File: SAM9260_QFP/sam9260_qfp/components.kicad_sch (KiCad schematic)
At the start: 64 parts, among them J201 USB_B_Micro, J202 Micro_SD_Card, J203 RJ45, U201 USBLC6-2SC6, U202 LD1117S33TR_SOT223, U203 RTL8211EG-VB-CG, Y201 25Mhz

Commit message: Completed component placing
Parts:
- added C235: 100n, Capacitor_SMD:C_0402_1005Metric, symbol Device:C_Small
- FB201: footprint Inductor_SMD:L_0805_2012Metric -> Inductor_SMD:L_0603_1608Metric
- XMER201: footprint My_First_PCB:H5007NL_PUL -> H5007NL:H5007NL_PUL
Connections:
- net GND is gone; now on net +1V0: C201.2, C202.2, C203.2, C204.2, C205.2, C206.2, C207.2, C208.2, C209.2, C210.2, C211.2, C212.2, C213.2, C214.2, C215.2, C216.2, C217.2, C218.1, C219.2, C220.2, C221.2, C222.2, C223.2, C224.2, C225.1, C226.1, C226.2, C227.2, C228.1, C228.2, C229.2, C230.2, C231.2, C232.2, C233.2, C234.2, J201.5 (GND), J201.6 (Shield), J202.4 (VDD), J202.6 (VSS), L201.2, R203.1, R206.2, R207.2, U201.2 (GND), U202.1 (GND), U203.10 (AVDD33), U203.13 (AVDD10), U203.2 (GND), U203.20 (DVDD33), U203.26 (DVDD33), U203.33 (DVDD10), U203.37 (DVDD33), U203.4 (GND), U203.48 (DVDD10), U203.49 (DVDD33), U203.59 (AVDD10), U203.60 (AVDD33), U203.63 (GND), U203.64 (VDDREG), U203.65 (GND), U203.7 (AVDD10)
- net +1V0: now reaches C220.1, C223.1, C227.1
- net +1V0: now also C229.1, C230.1, C231.1, C235.1, C235.2
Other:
- moved on the sheet: C220, C223, C227

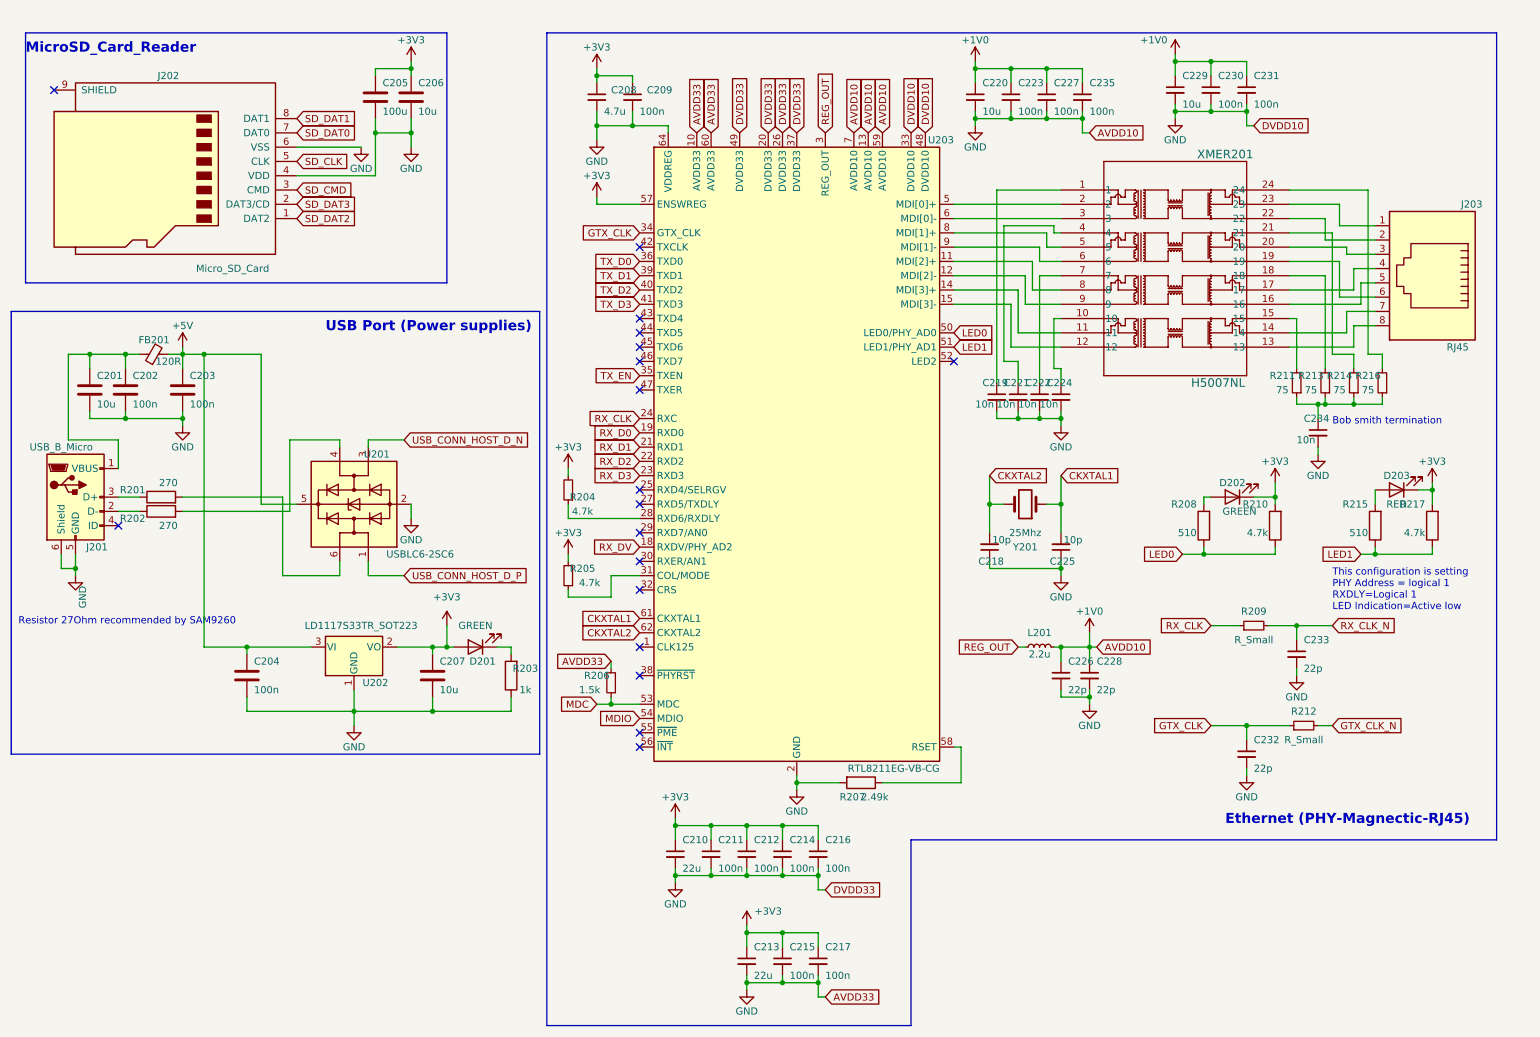
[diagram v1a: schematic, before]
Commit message: updated layout
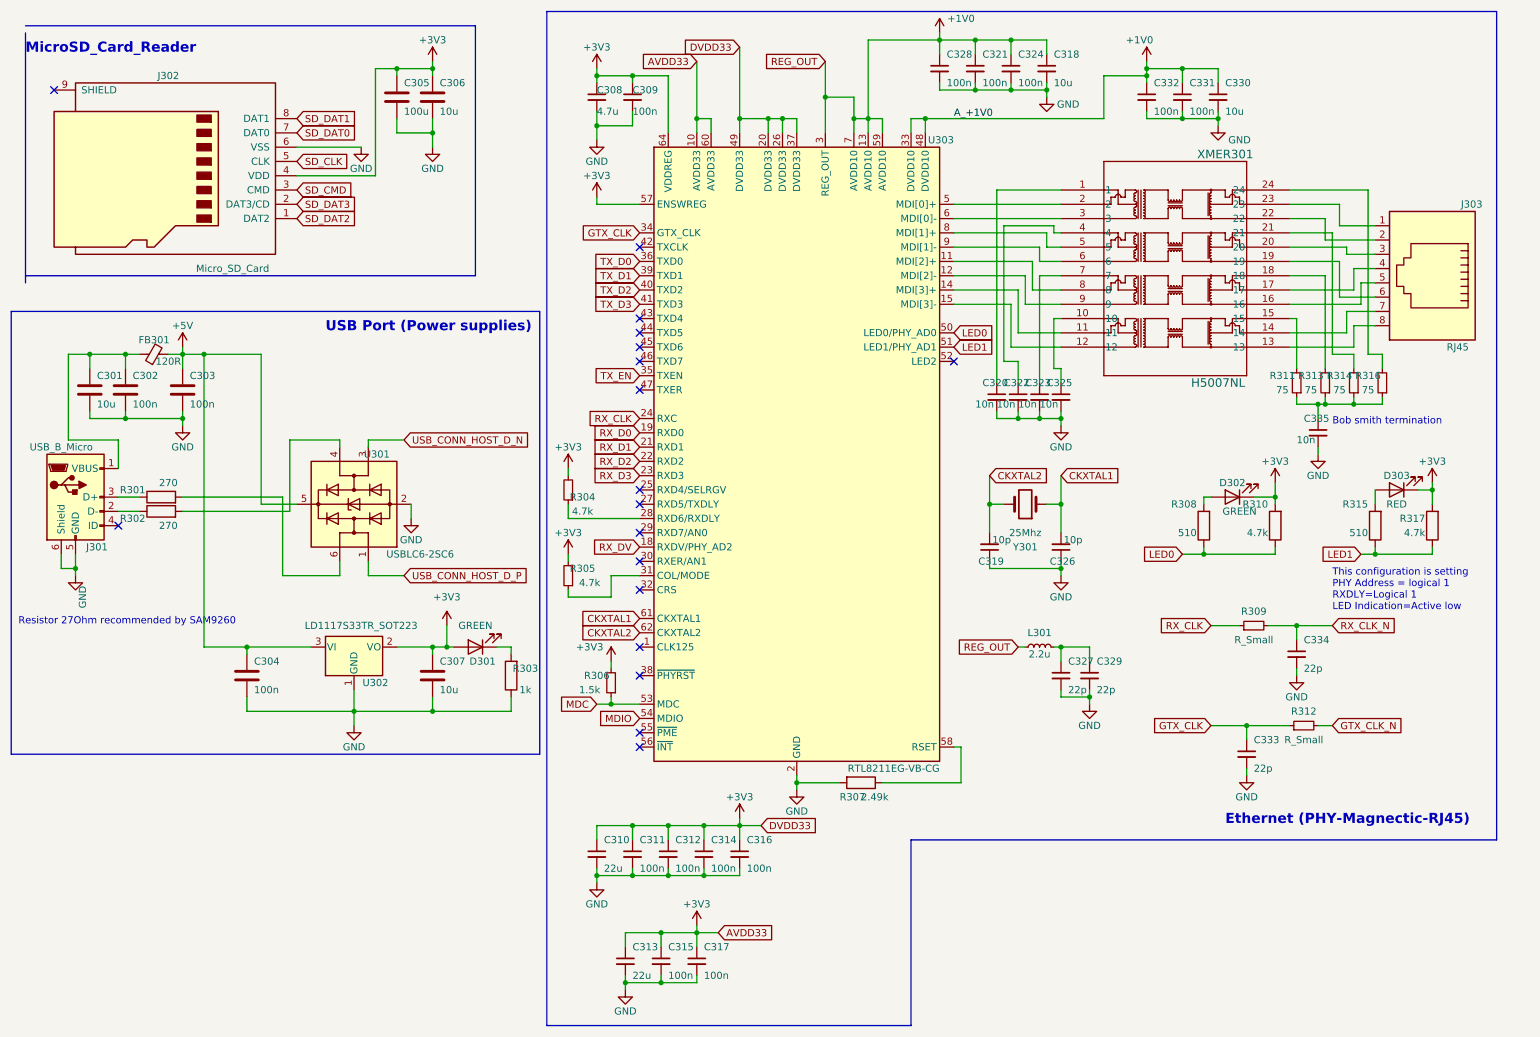
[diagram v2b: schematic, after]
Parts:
- XMER301: renamed from XMER201; footprint H5007NL:H5007NL_PUL -> HL5007:H5007NL_PUL
- renumbered C201 to C301, C202 to C302, C203 to C303, C204 to C304, C205 to C305, C206 to C306, C207 to C307, C208 to C308, C209 to C309, C210 to C310, C211 to C311, C212 to C312, C213 to C313, C214 to C314, C215 to C315, C216 to C316, C217 to C317, C220 to C318, C218 to C319, C219 to C320, C223 to C321, C221 to C322, C222 to C323, C227 to C324, C224 to C325, C225 to C326, C226 to C327, C235 to C328, C228 to C329, C229 to C330, C230 to C331, C231 to C332, C232 to C333, C233 to C334, C234 to C335, D201 to D301, D202 to D302, D203 to D303, FB201 to FB301, J201 to J301, J202 to J302, J203 to J303, L201 to L301, R201 to R301, R202 to R302, R203 to R303, R204 to R304, R205 to R305, R206 to R306, R207 to R307, R208 to R308, R209 to R309, R210 to R310, R211 to R311, R212 to R312, R213 to R313, R214 to R314, R215 to R315, R216 to R316, R217 to R317, U201 to U301, U202 to U302, U203 to U303, Y201 to Y301
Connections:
- net REG_OUT is gone; now on net +1V0: L301.1, U303.3 (REG_OUT)
- net +1V0: no longer C301.2, C302.2, C303.2, C304.2, C305.2, C306.2, C307.2, C308.2, C309.2, C310.2, C311.2, C312.2, C313.2, C314.2, C315.2, C316.2, C317.2, C318.2, C319.1, C320.2, C321.2, C322.2, C323.2, C324.2, C325.2, C326.1, C327.1, C327.2, C328.2, C329.1, C329.2, C330.2, C331.2, C332.2, C333.2, C334.2, C335.2, J301.5 (GND), J301.6 (Shield), J302.4 (VDD), J302.6 (VSS), L301.2, R303.1, R306.2, R307.2, U301.2 (GND), U302.1 (GND), U303.10 (AVDD33), U303.2 (GND), U303.20 (DVDD33), U303.26 (DVDD33), U303.37 (DVDD33), U303.4 (GND), U303.49 (DVDD33), U303.60 (AVDD33), U303.63 (GND), U303.64 (VDDREG), U303.65 (GND)
- net +3V3: now also J302.4 (VDD), R306.2, U303.10 (AVDD33), U303.20 (DVDD33), U303.26 (DVDD33), U303.37 (DVDD33), U303.49 (DVDD33), U303.60 (AVDD33), U303.64 (VDDREG)
- new net: C327.1, C329.1, L301.2
- new net GND: C301.2, C302.2, C303.2, C304.2, C305.2, C306.2, C307.2, C308.2, C309.2, C310.2, C311.2, C312.2, C313.2, C314.2, C315.2, C316.2, C317.2, C318.2, C319.1, C320.2, C321.2, C322.2, C323.2, C324.2, C325.2, C326.1, C327.2, C328.2, C329.2, C330.2, C331.2, C332.2, C333.2, C334.2, C335.2, J301.5 (GND), J301.6 (Shield), J302.6 (VSS), R303.1, R307.2, U301.2 (GND), U302.1 (GND), U303.2 (GND), U303.4 (GND), U303.63 (GND), U303.65 (GND)
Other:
- moved on the sheet: C305, C306, C310, C311, C312, C313, C314, C315, C316, C317, C318, C321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

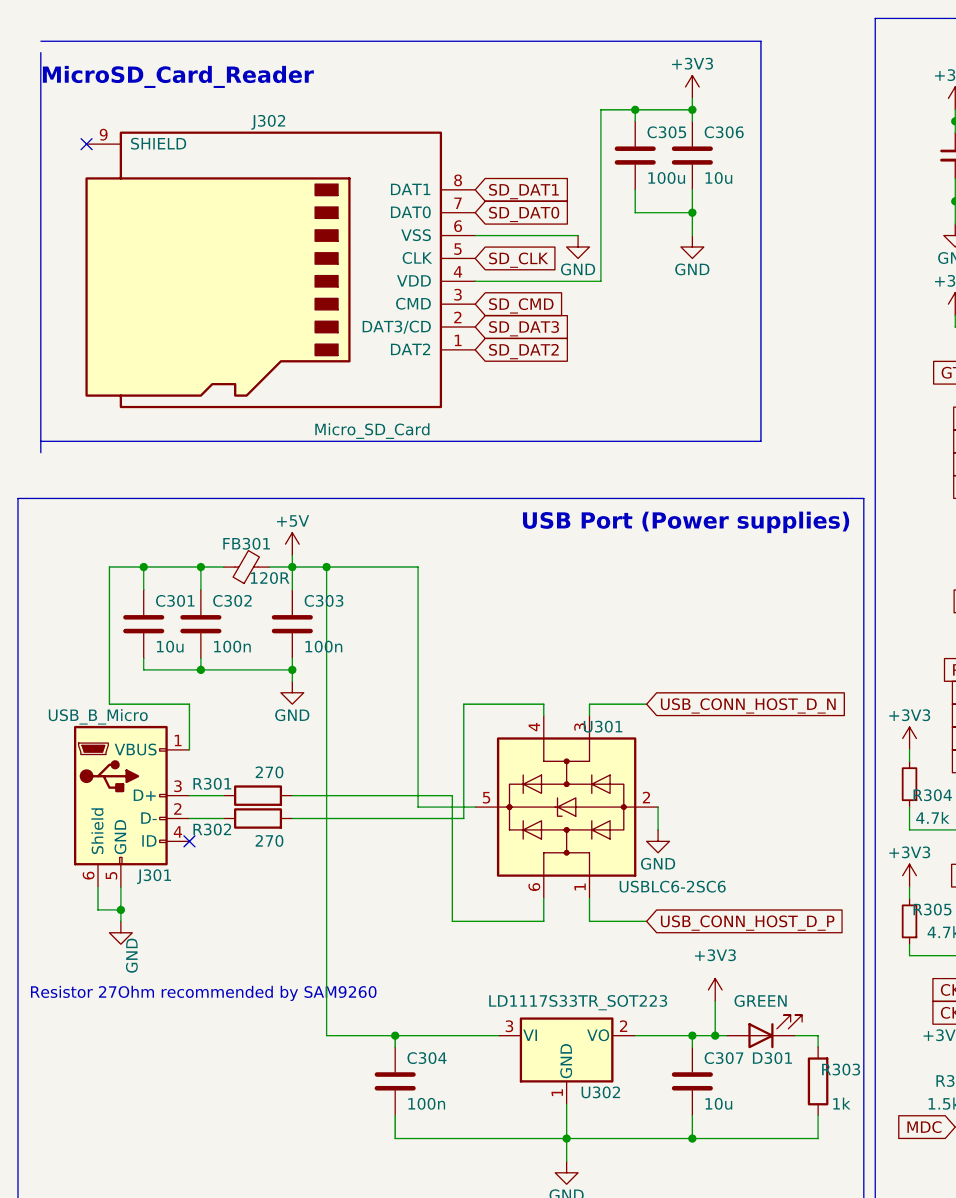
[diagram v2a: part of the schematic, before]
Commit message: Completed routing, need to add logo
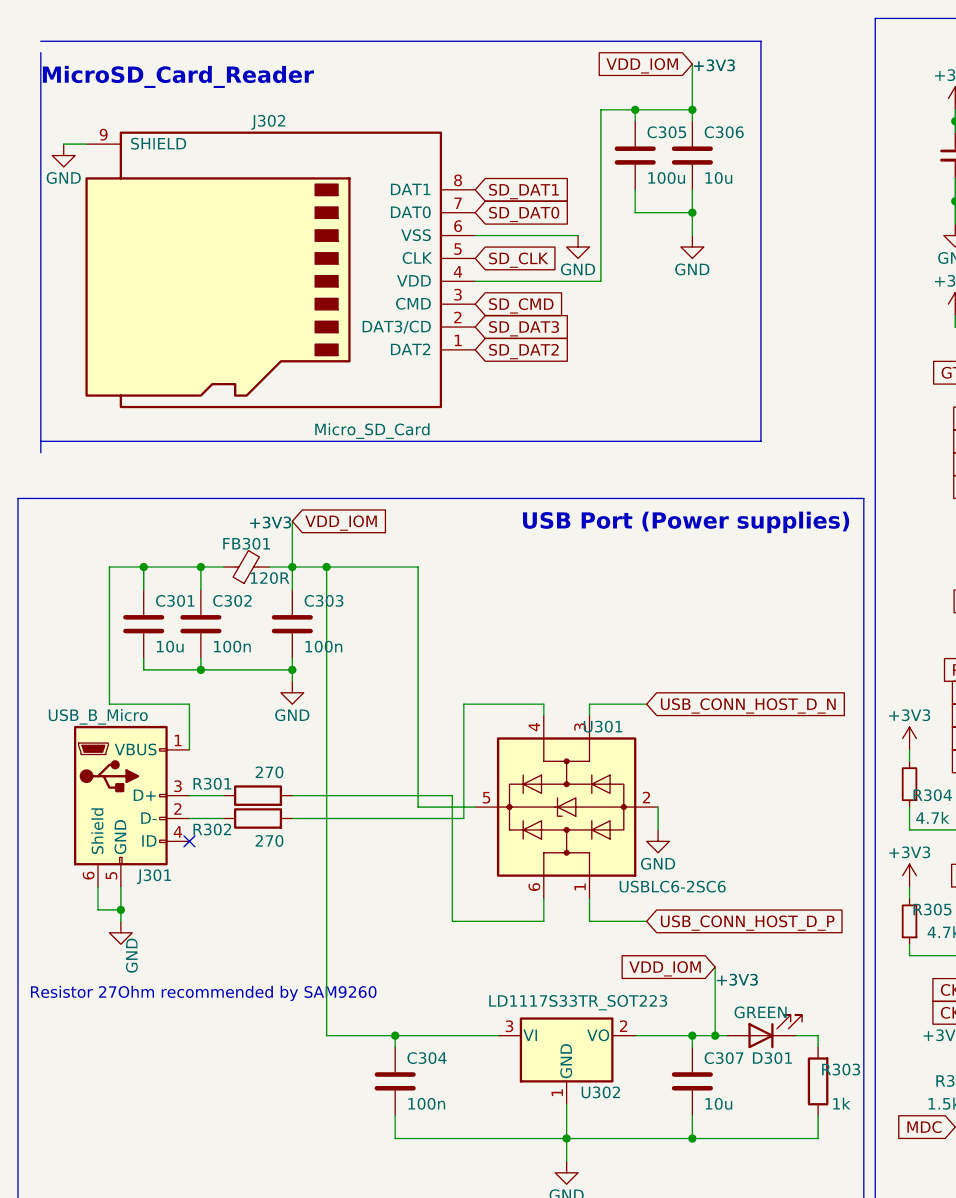
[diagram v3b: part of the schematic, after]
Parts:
- XMER301: footprint HL5007:H5007NL_PUL -> H5007NL:H5007NL_PUL
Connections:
- net +5V is gone; now on net +3V3: C303.1, C304.1, FB301.2, U301.5 (VBUS), U302.3 (VI)
- net GND: now also J302.9 (SHIELD)
- no-connect marks 18 -> 17
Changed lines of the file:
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@@
   (no_connect (at 127 106.68))
   (no_connect (at 127 101.6))
-  (no_connect (at 22.86 27.94))
   (no_connect (at 127 132.08))
   (no_connect (at 127 55.88))
@@
     (stroke (width 0) (type default))
   )
-  (wire (pts (xy 45.72 73.66) (xy 45.72 74.93))
+  (wire (pts (xy 45.72 69.85) (xy 45.72 74.93))
     (stroke (width 0) (type default))
   )
@@
     (stroke (width 0) (type default))
   )
-  (wire (pts (xy 92.71 123.19) (xy 92.71 127))
+  (wire (pts (xy 92.71 119.38) (xy 92.71 127))
     (stroke (width 0) (type default))
   )
@@
     (stroke (width 0) (type default))
   )
-  (wire (pts (xy 90.17 22.86) (xy 90.17 24.13))
+  (wire (pts (xy 90.17 19.05) (xy 90.17 24.13))
     (stroke (width 0) (type default))
   )
@@
     (stroke (width 0) (type default))
   )
+  (wire (pts (xy 20.32 27.94) (xy 22.86 27.94))
+    (stroke (width 0) (type default))
+  )
   (wire (pts (xy 228.6 123.19) (xy 233.68 123.19))
     (stroke (width 0) (type default))
@@
     (effects (font (size 1.27 1.27)) (justify left bottom))
   )
+  (label "+3V3" (at 90.17 20.32 0) (fields_autoplaced)
+    (effects (font (size 1.27 1.27)) (justify left bottom))
+  )
+  (label "+3V3" (at 92.71 121.92 0) (fields_autoplaced)
+    (effects (font (size 1.27 1.27)) (justify left bottom))
+  )
+  (label "+3V3" (at 45.72 71.12 180) (fields_autoplaced)
+    (effects (font (size 1.27 1.27)) (justify right bottom))
+  )
   (global_label "REG_OUT" (shape input) (at 160.02 22.86 180) (fields_autoplaced)
     (effects (font (size 1.27 1.27)) (justify right))
@@
     )
   )
+  (global_label "VDD_IOM" (shape input) (at 92.71 119.38 180) (fields_autoplaced)
+    (effects (font (size 1.27 1.27)) (justify right))
+    (property "Intersheetrefs" "${INTERSHEET_REFS}" (at 81.7419 119.38 0)
+      (effects (font (size 1.27 1.27)) (justify right) hide)
+    )
+  )
   (global_label "RX_D1" (shape input) (at 127 91.44 180) (fields_autoplaced)
     (effects (font (size 1.27 1.27)) (justify right))
@@
     )
   )
+  (global_label "VDD_IOM" (shape input) (at 90.17 19.05 180) (fields_autoplaced)
+    (effects (font (size 1.27 1.27)) (justify right))
+    (property "Intersheetrefs" "${INTERSHEET_REFS}" (at 79.2019 19.05 0)
+      (effects (font (size 1.27 1.27)) (justify right) hide)
+    )
+  )
   (global_label "RX_DV" (shape input) (at 127 109.22 180) (fields_autoplaced)
     (effects (font (size 1.27 1.27)) (justify right))
@@
     )
   )
+  (global_label "VDD_IOM" (shape input) (at 45.72 69.85 0) (fields_autoplaced)
+    (effects (font (size 1.27 1.27)) (justify left))
+    (property "Intersheetrefs" "${INTERSHEET_REFS}" (at 56.6881 69.85 0)
+      (effects (font (size 1.27 1.27)) (justify left) hide)
+    )
+  )
   (global_label "TX_D1" (shape input) (at 127 60.96 180) (fields_autoplaced)
     (effects (font (size 1.27 1.27)) (justify right))
@@
     )
   )
-  (symbol (lib_id "power:+5V") (at 45.72 73.66 0) (unit 1)
-    (in_bom yes) (on_board yes) (dnp no)
-    (property "Reference" "#PWR0202" (at 45.72 77.47 0)
-      (effects (font (size 1.27 1.27)) hide)
-    )
-    (property "Value" "+5V" (at 45.72 69.85 0)
-      (effects (font (size 1.27 1.27)))
-    )
-    (property "Footprint" "" (at 45.72 73.66 0)
-      (effects (font (size 1.27 1.27)) hide)
-    )
-    (property "Datasheet" "" (at 45.72 73.66 0)
-      (effects (font (size 1.27 1.27)) hide)
-    )
-    (pin "1")
-    (instances
-      (project "sam9260_qfp"
-        (path "/e0cfbfe5-8f1c-42d1-90c4-1cf34dee8164/c38b7e9d-1aca-474d-b327-b31e7c88c3d1"
-          (reference "#PWR0202") (unit 1)
-        )
-      )
-    )
-  )
   (symbol (lib_id "power:+3V3") (at 137.16 176.53 0) (unit 1)
     (in_bom yes) (on_board yes) (dnp no)
@@
     )
   )
-  (symbol (lib_id "power:+3V3") (at 90.17 22.86 0) (unit 1)
-    (in_bom yes) (on_board yes) (dnp no)
-    (property "Reference" "#PWR0203" (at 90.17 26.67 0)
-      (effects (font (size 1.27 1.27)) hide)
-    )
-    (property "Value" "+3V3" (at 90.17 19.05 0)
-      (effects (font (size 1.27 1.27)))
-    )
-    (property "Footprint" "" (at 90.17 22.86 0)
-      (effects (font (size 1.27 1.27)) hide)
-    )
-    (property "Datasheet" "" (at 90.17 22.86 0)
-      (effects (font (size 1.27 1.27)) hide)
-    )
-    (pin "1")
-    (instances
-      (project "sam9260_qfp"
-        (path "/e0cfbfe5-8f1c-42d1-90c4-1cf34dee8164/c38b7e9d-1aca-474d-b327-b31e7c88c3d1"
-          (reference "#PWR0203") (unit 1)
-        )
-      )
-    )
-  )
   (symbol (lib_id "power:GND") (at 229.87 34.29 0) (unit 1)
     (in_bom yes) (on_board yes) (dnp no)
@@
     )
   )
+  (symbol (lib_id "power:GND") (at 20.32 27.94 0) (unit 1)
+    (in_bom yes) (on_board yes) (dnp no)
+    (property "Reference" "#PWR0222" (at 20.32 34.29 0)
+      (effects (font (size 1.27 1.27)) hide)
+    )
+    (property "Value" "GND" (at 20.32 31.75 0)
+      (effects (font (size 1.27 1.27)))
+    )
+    (property "Footprint" "" (at 20.32 27.94 0)
+      (effects (font (size 1.27 1.27)) hide)
+    )
+    (property "Datasheet" "" (at 20.32 27.94 0)
+      (effects (font (size 1.27 1.27)) hide)
+    )
+    (pin "1")
+    (instances
+      (project "sam9260_qfp"
+        (path "/e0cfbfe5-8f1c-42d1-90c4-1cf34dee8164/c38b7e9d-1aca-474d-b327-b31e7c88c3d1"
+          (reference "#PWR0222") (unit 1)
+        )
+      )
+    )
+  )
   (symbol (lib_id "power:GND") (at 201.93 87.63 0) (unit 1)
     (in_bom yes) (on_board yes) (dnp no)
@@
       (effects (font (size 1.524 1.524)))
     )
-    (property "Footprint" "HL5007:H5007NL_PUL" (at 201.93 45.72 0)
+    (property "Footprint" "H5007NL:H5007NL_PUL" (at 201.93 45.72 0)
       (effects (font (size 1.27 1.27) italic) hide)
     )
@@
     )
   )
-  (symbol (lib_id "power:+3V3") (at 92.71 123.19 0) (unit 1)
-    (in_bom yes) (on_board yes) (dnp no) (fields_autoplaced)
-    (property "Reference" "#PWR0198" (at 92.71 127 0)
-      (effects (font (size 1.27 1.27)) hide)
-    )
-    (property "Value" "+3V3" (at 92.71 118.11 0)
-      (effects (font (size 1.27 1.27)))
-    )
-    (property "Footprint" "" (at 92.71 123.19 0)
-      (effects (font (size 1.27 1.27)) hide)
-    )
-    (property "Datasheet" "" (at 92.71 123.19 0)
-      (effects (font (size 1.27 1.27)) hide)
-    )
-    (pin "1")
-    (instances
-      (project "sam9260_qfp"
-        (path "/e0cfbfe5-8f1c-42d1-90c4-1cf34dee8164/c38b7e9d-1aca-474d-b327-b31e7c88c3d1"
-          (reference "#PWR0198") (unit 1)
-        )
-      )
-    )
-  )
   (symbol (lib_id "power:+3V3") (at 114.3 110.49 0) (unit 1)
     (in_bom yes) (on_board yes) (dnp no)
@@
       (effects (font (size 1.27 1.27)))
     )
-    (property "Value" "GREEN" (at 97.79 123.19 0)
+    (property "Value" "GREEN" (at 97.79 124.46 0)
       (effects (font (size 1.27 1.27)))
     )

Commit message: Added logo
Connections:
- net +3V3: now also D302.2 (A), D303.2 (A); no longer D302.1 (K), D303.1 (K)
- net at R315.2: now also D303.1 (K); no longer D303.2 (A)
- net at R308.2: now also D302.1 (K); no longer D302.2 (A)
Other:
- moved on the sheet: D302, D303
